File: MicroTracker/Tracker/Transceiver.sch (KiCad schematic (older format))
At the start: 4 parts, among them IC1 RN2483A-I_RM105, J2 Conn_Coaxial, U5 RFM95W-868S2

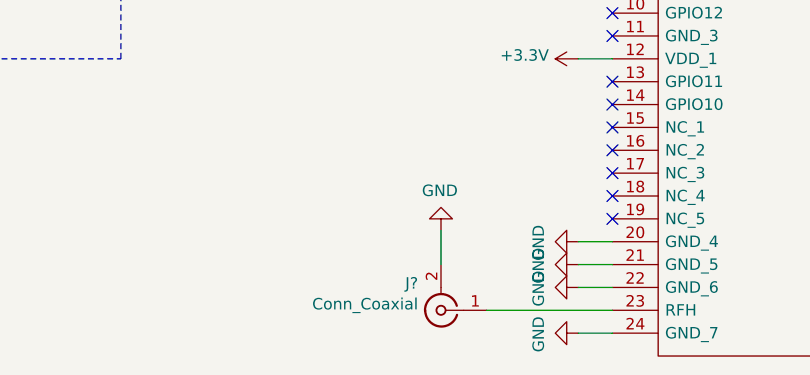
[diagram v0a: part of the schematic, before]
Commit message: added charges
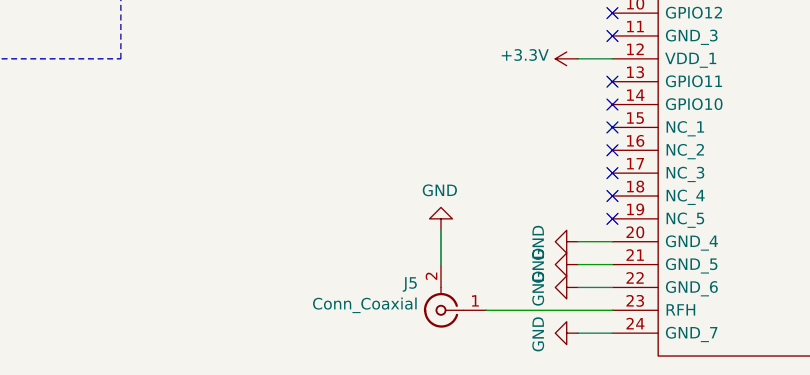
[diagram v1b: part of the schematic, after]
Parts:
- gave numbers to parts that had none: 1
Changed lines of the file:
@@
 $EndComp
 $Comp
-L power:GND #PWR?
+L power:GND #PWR0133
 U 1 1 5EF9599C
 P 9150 2450
-F 0 "#PWR?" H 9150 2200 50  0001 C CNN
+F 0 "#PWR0133" H 9150 2200 50  0001 C CNN
 F 1 "GND" H 9155 2277 50  0000 C CNN
 F 2 "" H 9150 2450 50  0001 C CNN
@@
 	9000 2450 9150 2450
 $Comp
-L power:GND #PWR?
+L power:GND #PWR0134
 U 1 1 5EF96B57
 P 9150 2550
-F 0 "#PWR?" H 9150 2300 50  0001 C CNN
+F 0 "#PWR0134" H 9150 2300 50  0001 C CNN
 F 1 "GND" H 9155 2377 50  0000 C CNN
 F 2 "" H 9150 2550 50  0001 C CNN
@@
 	9000 2550 9150 2550
 $Comp
-L power:GND #PWR?
+L power:GND #PWR0135
 U 1 1 5EF96F55
 P 9150 2650
-F 0 "#PWR?" H 9150 2400 50  0001 C CNN
+F 0 "#PWR0135" H 9150 2400 50  0001 C CNN
 F 1 "GND" H 9155 2477 50  0000 C CNN
 F 2 "" H 9150 2650 50  0001 C CNN
@@
 	9000 2650 9150 2650
 $Comp
-L power:GND #PWR?
+L power:GND #PWR0136
 U 1 1 5EF977D6
 P 7250 2350
-F 0 "#PWR?" H 7250 2100 50  0001 C CNN
+F 0 "#PWR0136" H 7250 2100 50  0001 C CNN
 F 1 "GND" H 7255 2177 50  0000 C CNN
 F 2 "" H 7250 2350 50  0001 C CNN
@@
 	7400 2350 7250 2350
 $Comp
-L power:GND #PWR?
+L power:GND #PWR0137
 U 1 1 5EF97F0A
 P 7250 3050
-F 0 "#PWR?" H 7250 2800 50  0001 C CNN
+F 0 "#PWR0137" H 7250 2800 50  0001 C CNN
 F 1 "GND" H 7255 2877 50  0000 C CNN
 F 2 "" H 7250 3050 50  0001 C CNN
@@
 	7400 3050 7250 3050
 $Comp
-L power:GND #PWR?
+L power:GND #PWR0138
 U 1 1 5EF98398
 P 7250 4250
-F 0 "#PWR?" H 7250 4000 50  0001 C CNN
+F 0 "#PWR0138" H 7250 4000 50  0001 C CNN
 F 1 "GND" H 7255 4077 50  0000 C CNN
 F 2 "" H 7250 4250 50  0001 C CNN
@@
 	7400 4250 7250 4250
 $Comp
-L power:GND #PWR?
+L power:GND #PWR0139
 U 1 1 5EF98889
 P 7250 4350
-F 0 "#PWR?" H 7250 4100 50  0001 C CNN
+F 0 "#PWR0139" H 7250 4100 50  0001 C CNN
 F 1 "GND" H 7255 4177 50  0000 C CNN
 F 2 "" H 7250 4350 50  0001 C CNN
@@
 	7400 4350 7250 4350
 $Comp
-L power:GND #PWR?
+L power:GND #PWR0140
 U 1 1 5EF98ECA
 P 7250 4450
-F 0 "#PWR?" H 7250 4200 50  0001 C CNN
+F 0 "#PWR0140" H 7250 4200 50  0001 C CNN
 F 1 "GND" H 7255 4277 50  0000 C CNN
 F 2 "" H 7250 4450 50  0001 C CNN
@@
 	7400 4450 7250 4450
 $Comp
-L power:GND #PWR?
+L power:GND #PWR0141
 U 1 1 5EF99598
 P 7250 4650
-F 0 "#PWR?" H 7250 4400 50  0001 C CNN
+F 0 "#PWR0141" H 7250 4400 50  0001 C CNN
 F 1 "GND" H 7255 4477 50  0000 C CNN
 F 2 "" H 7250 4650 50  0001 C CNN
@@
 	7400 4650 7250 4650
 $Comp
-L power:GND #PWR?
+L power:GND #PWR0142
 U 1 1 5EF99F8A
 P 9150 4550
-F 0 "#PWR?" H 9150 4300 50  0001 C CNN
+F 0 "#PWR0142" H 9150 4300 50  0001 C CNN
 F 1 "GND" H 9155 4377 50  0000 C CNN
 F 2 "" H 9150 4550 50  0001 C CNN
@@
 	9000 4550 9150 4550
 $Comp
-L power:GND #PWR?
+L power:GND #PWR0143
 U 1 1 5EF9AB08
 P 9150 3950
-F 0 "#PWR?" H 9150 3700 50  0001 C CNN
+F 0 "#PWR0143" H 9150 3700 50  0001 C CNN
 F 1 "GND" H 9155 3777 50  0000 C CNN
 F 2 "" H 9150 3950 50  0001 C CNN
@@
 	9000 3950 9150 3950
 $Comp
-L power:GND #PWR?
+L power:GND #PWR0144
 U 1 1 5EF9B0E6
 P 9150 3150
-F 0 "#PWR?" H 9150 2900 50  0001 C CNN
+F 0 "#PWR0144" H 9150 2900 50  0001 C CNN
 F 1 "GND" H 9155 2977 50  0000 C CNN
 F 2 "" H 9150 3150 50  0001 C CNN
@@
 	9000 3150 9150 3150
 $Comp
-L Connector:Conn_Coaxial J?
+L Connector:Conn_Coaxial J5
 U 1 1 5EF9B779
 P 6650 4550
-F 0 "J?" H 6750 4432 50  0000 L CNN
+F 0 "J5" H 6750 4432 50  0000 L CNN
 F 1 "Conn_Coaxial" H 6750 4523 50  0000 L CNN
 F 2 "" H 6650 4550 50  0001 C CNN
@@
 $EndComp
 $Comp
-L power:GND #PWR?
+L power:GND #PWR0145
 U 1 1 5EF9D9EA
 P 6650 4200
-F 0 "#PWR?" H 6650 3950 50  0001 C CNN
+F 0 "#PWR0145" H 6650 3950 50  0001 C CNN
 F 1 "GND" H 6655 4027 50  0000 C CNN
 F 2 "" H 6650 4200 50  0001 C CNN
@@
 	7250 2850 7400 2850
 $Comp
-L power:+3.3V #PWR?
+L power:+3.3V #PWR0146
 U 1 1 5EFA01D1
 P 7250 3450
-F 0 "#PWR?" H 7250 3300 50  0001 C CNN
+F 0 "#PWR0146" H 7250 3300 50  0001 C CNN
 F 1 "+3.3V" V 7265 3578 50  0000 L CNN
 F 2 "" H 7250 3450 50  0001 C CNN
@@
 	7250 3450 7400 3450
 $Comp
-L power:+3.3V #PWR?
+L power:+3.3V #PWR0147
 U 1 1 5EFA29CB
 P 9150 3250
-F 0 "#PWR?" H 9150 3100 50  0001 C CNN
+F 0 "#PWR0147" H 9150 3100 50  0001 C CNN
 F 1 "+3.3V" V 9165 3378 50  0000 L CNN
 F 2 "" H 9150 3250 50  0001 C CNN

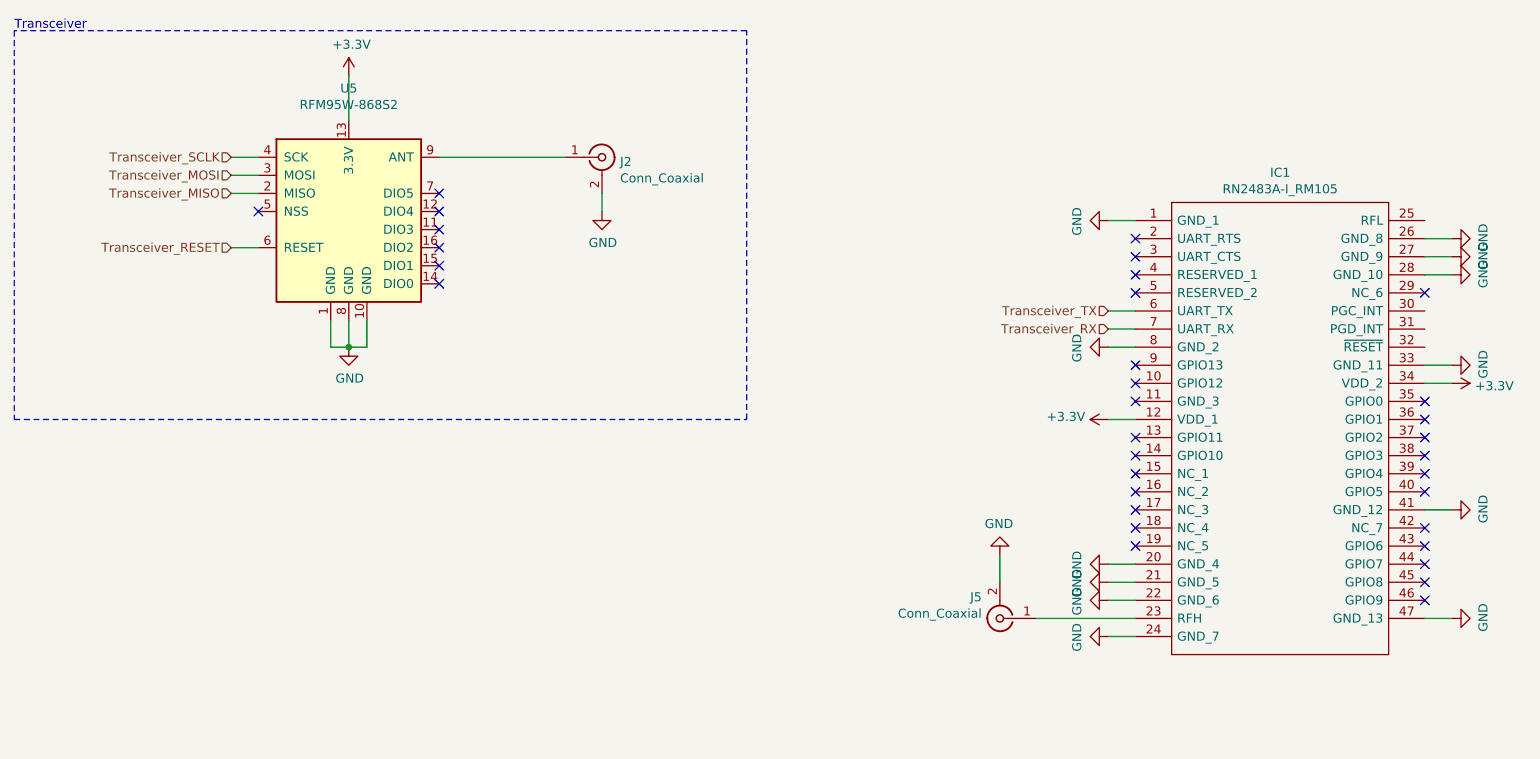
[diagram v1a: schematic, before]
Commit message: added more parts and lib
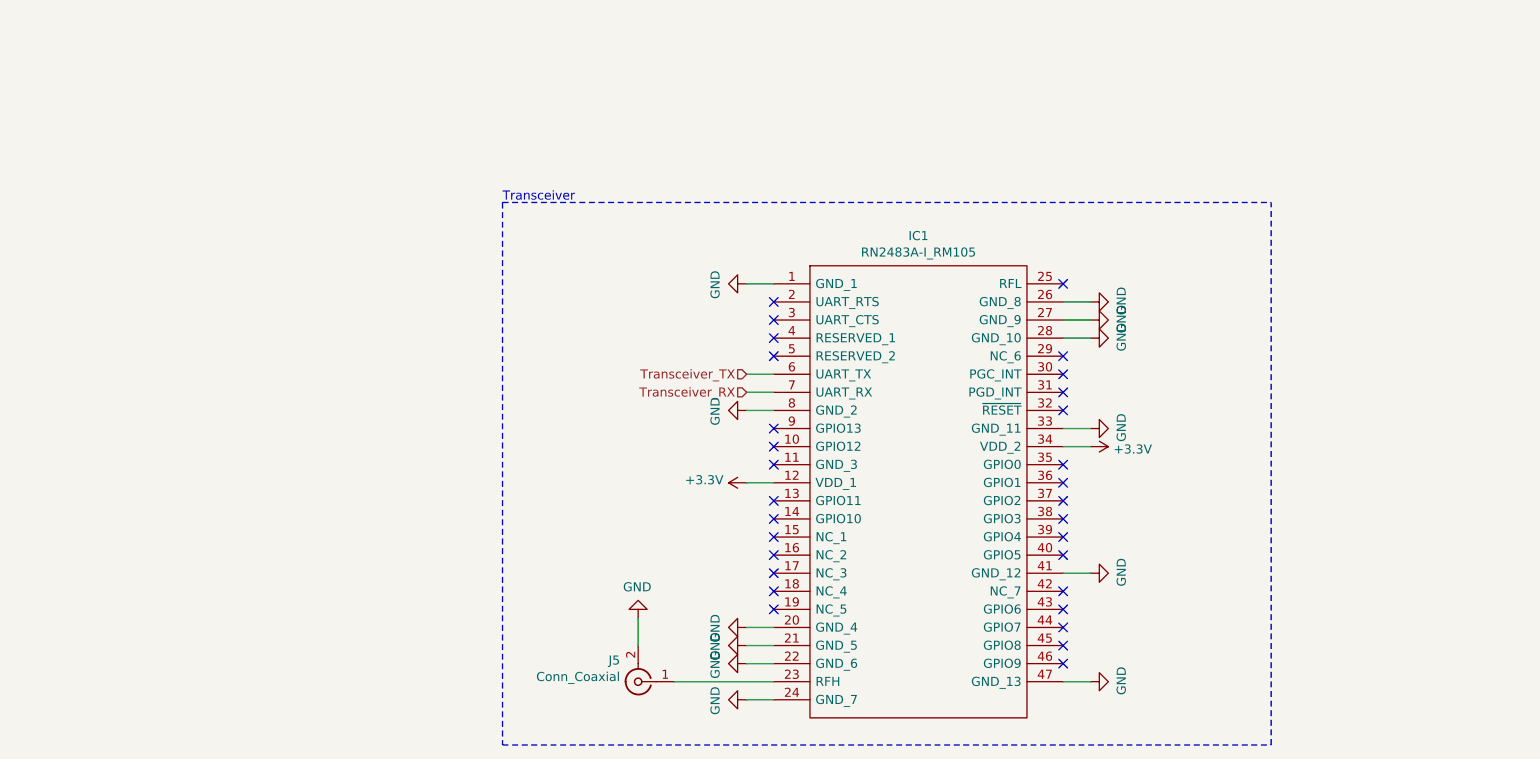
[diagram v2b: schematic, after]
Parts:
- removed J2: Conn_Coaxial, symbol Connector:Conn_Coaxial
- removed U5: RFM95W-868S2, symbol RF_Module:RFM95W-868S2
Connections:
- no-connect marks 33 -> 30
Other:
- moved on the sheet: IC1, J5
